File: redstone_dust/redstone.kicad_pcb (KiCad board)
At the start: 2 copper layers, 40 x 40 mm, 76 parts, among them J1 1x4_Pogo, J2 1x4_Pogo, J3 1x4_Pogo, J4 1x4_Pogo, J5 1x4_Pogo, J6 1x4_Pogo, J7 1x4_Pogo, J8 1x4_Pogo, SW1 SW_Push_Open, U1 RP2040

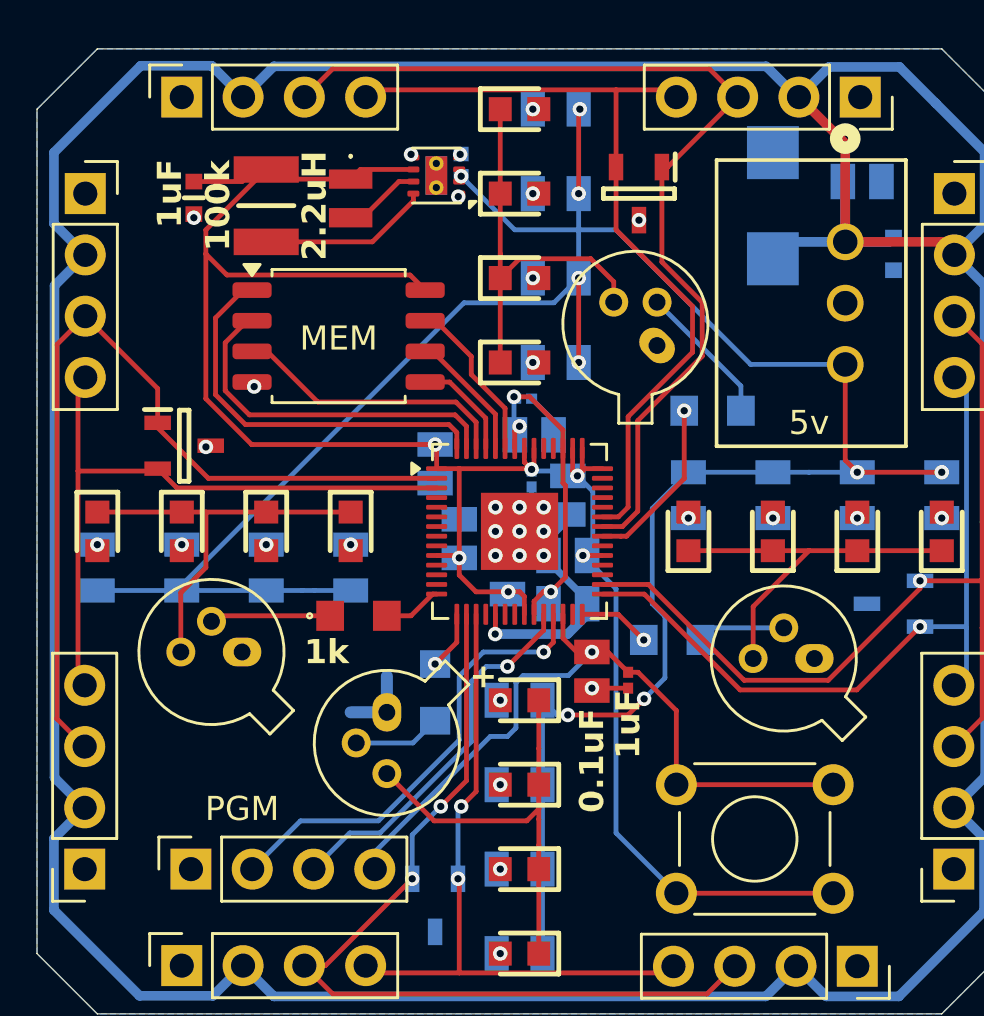
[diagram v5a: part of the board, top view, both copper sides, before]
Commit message: change programming pin 4 to 3.3v
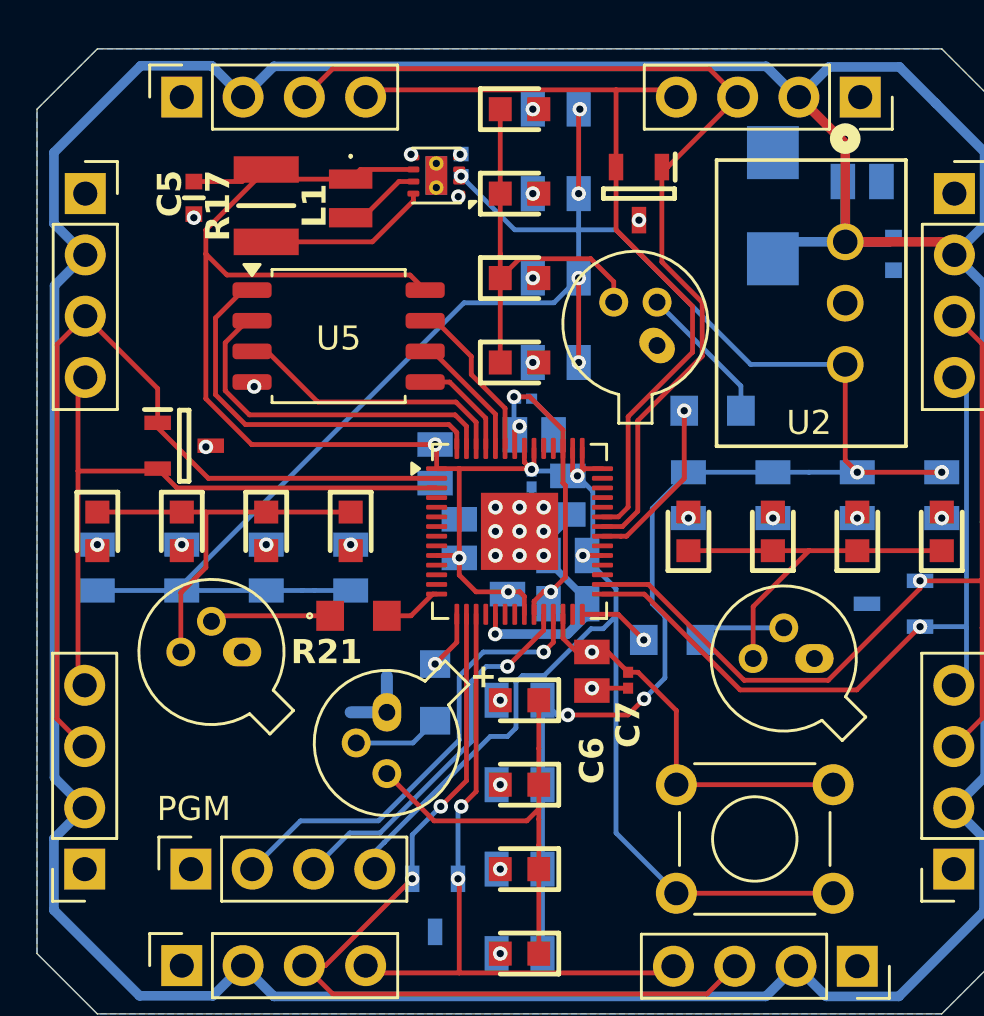
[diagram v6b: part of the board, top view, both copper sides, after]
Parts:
- D5: renamed from - LED +
- D9: renamed from + LED -
- renumbered 10uF to C1, 0.1uF to C2, 0.1uF to C3, 22uF to C4, 1uF to C5, 0.1uF to C6, 1uF to C7, TVS to D19, 2.2uH to L1, BC108 to Q1, BC108 to Q2, BC108 to Q3, BC108 to Q4, 200 to R1, 200 to R11, 200 to R15, 100k to R17, 1k to R18, 1k to R19, 1k to R20, 1k to R21, 200 to R6, 5v to U2, 3.3v to U3, MEM to U5
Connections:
- C6 pad 1: Net-(J9-Pin_4) -> Net-(SW1-B)
- C7 pad 1: Net-(J9-Pin_4) -> Net-(SW1-B)
- PGM pad 4: Net-(J9-Pin_4) -> /3.3V_LOCAL
- SW1 pad 2: Net-(J9-Pin_4) -> Net-(SW1-B)
- U1 pad 26: Net-(J9-Pin_4) -> Net-(SW1-B)
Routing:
- net Net-(J9-Pin_4): track 30.8 -> 0.00 mm, vias 1 -> 0
- net Net-(SW1-B): track 0.00 -> 16.5 mm, vias 0 -> 1
- net /3.3V_LOCAL: track 88.1 -> 104.0 mm
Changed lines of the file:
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@@
 	(net 70 "Net-(U1-GPIO12)")
 	(net 71 "unconnected-(U1-GPIO16-Pad27)")
-	(net 72 "Net-(J9-Pin_4)")
+	(net 72 "Net-(SW1-B)")
 	(net 73 "unconnected-(U1-GPIO9-Pad12)")
 	(net 74 "unconnected-(U1-GPIO8-Pad11)")
@@
 		(descr "150060RS83000")
 		(tags "LED")
-		(property "Reference" "- LED +"
+		(property "Reference" "D5"
 			(at 0 1.5 90)
 			(layer "F.SilkS")
@@
 		(at 148.5 43 -90)
 		(tags "RBT05W24S05 ")
-		(property "Reference" "5v"
+		(property "Reference" "U2"
 			(at 7.5 1.5 0)
 			(unlocked yes)
@@
 			(layers "*.Cu" "*.Mask")
 			(remove_unused_layers no)
-			(net 72 "Net-(J9-Pin_4)")
+			(net 72 "Net-(SW1-B)")
 			(pinfunction "B")
 			(pintype "passive")
@@
 			(layers "*.Cu" "*.Mask")
 			(remove_unused_layers no)
-			(net 72 "Net-(J9-Pin_4)")
+			(net 72 "Net-(SW1-B)")
 			(pinfunction "B")
 			(pintype "passive")
@@
 		(descr "8-Lead Plastic WSON, 2x2mm Body, 0.5mm Pitch, WSON-8, http://www.ti.com/lit/ds/symlink/lm27761.pdf")
 		(tags "WSON 8 1EP ThermalVias")
-		(property "Reference" "3.3v"
+		(property "Reference" "U3"
 			(at 0.05 1.75 0)
 			(layer "F.SilkS")
@@
 		(tags "Through hole socket strip THT 1x04 2.54mm single row")
 		(property "Reference" "PGM"
-			(at 2.5 2.12 180)
+			(at 2.5 0.12 180)
 			(layer "F.SilkS")
 			(effects
@@
 			(layers "*.Cu" "*.Mask")
 			(remove_unused_layers no)
-			(net 72 "Net-(J9-Pin_4)")
+			(net 3 "/3.3V_LOCAL")
 			(pinfunction "Pin_4")
 			(pintype "passive")
@@
 		(descr "GRM03_0.03 L=0.6mm W=0.3mm T=0.3mm")
 		(tags "Capacitor")
-		(property "Reference" "1uF"
+		(property "Reference" "C7"
 			(at 1.83 0 90)
 			(layer "F.SilkS")
@@
 			(size 0.42 0.46)
 			(layers "F.Cu" "F.Mask" "F.Paste")
-			(net 72 "Net-(J9-Pin_4)")
+			(net 72 "Net-(SW1-B)")
 			(pinfunction "1")
 			(pintype "passive")
@@
 		(descr "TO-18-3, generated with kicad-footprint-generator TO_SOT_THT_generate.py")
 		(tags "TO-18-3")
-		(property "Reference" "BC108"
+		(property "Reference" "Q2"
 			(at 1.221961 -1.73 0)
 			(layer "F.SilkS")
@@
 		(descr "LCENA2016MKT2R2M0NK-2")
 		(tags "Inductor")
-		(property "Reference" "2.2uH"
+		(property "Reference" "L1"
 			(at 0.3 1.5 90)
 			(layer "F.SilkS")
@@
 		(descr "ERJUP6")
 		(tags "Resistor")
-		(property "Reference" "1k"
+		(property "Reference" "R21"
 			(at -1.325 1.5 0)
 			(layer "F.SilkS")
@@
 		(descr "GRM18x")
 		(tags "Capacitor")
-		(property "Reference" "1uF"
+		(property "Reference" "C5"
 			(at -0.175 1 270)
 			(layer "F.SilkS")
@@
 		(descr "1210 (3225 Metric)")
 		(tags "Resistor")
-		(property "Reference" "100k"
+		(property "Reference" "R17"
 			(at 0 2 90)
 			(layer "F.SilkS")
@@
 		(descr "TO-18-3, generated with kicad-footprint-generator TO_SOT_THT_generate.py")
 		(tags "TO-18-3")
-		(property "Reference" "BC108"
+		(property "Reference" "Q1"
 			(at 1.411421 -0.992742 0)
 			(layer "F.SilkS")
@@
 		(descr "150060RS83000")
 		(tags "LED")
-		(property "Reference" "+ LED -"
+		(property "Reference" "D9"
 			(at 0 5 0)
 			(layer "F.SilkS")
@@
 		(descr "SOIC, 8 Pin (JEITA/EIAJ ED-7311-19 variation 08-001-BBA and Atmel/Microchip, 208 mils width, https://www.jeita.or.jp/japanese/standard/book/ED-7311-19/#target/page_no=21, https://ww1.microchip.com/downloads/en/DeviceDoc/20005045C.pdf#page=23, https://ww1.microchip.com/downloads/en/DeviceDoc/doc2535.pdf#page=162), generated with kicad-footprint-generator ipc_gullwing_generator.py")
 		(tags "SOIC SO P-SOP SOP SOP-8 SO SO-8 8S2 S2AE/F K04-056 CASE-751BE SO8W 8-Pin-SOIC PSA W8-2 W8-4 W8MS-1 FPT-8P-M08")
-		(property "Reference" "MEM"
+		(property "Reference" "U5"
 			(at 0 0.095 0)
 			(layer "F.SilkS")
@@
 			(layers "F.Cu" "F.Mask" "F.Paste")
 			(roundrect_rratio 0.25)
-			(net 72 "Net-(J9-Pin_4)")
+			(net 72 "Net-(SW1-B)")
 			(pinfunction "RUN")
 			(pintype "input")
@@
 		(descr "C0805F104K")
 		(tags "Capacitor")
-		(property "Reference" "0.1uF"
+		(property "Reference" "C6"
 			(at 3.7 0 270)
 			(layer "F.SilkS")
@@
 			(size 1.02 1.47)
 			(layers "F.Cu" "F.Mask" "F.Paste")
-			(net 72 "Net-(J9-Pin_4)")
+			(net 72 "Net-(SW1-B)")
 			(pinfunction "1")
 			(pintype "passive")
@@
 		(descr "TO-18-3, generated with kicad-footprint-generator TO_SOT_THT_generate.py")
 		(tags "TO-18-3")
-		(property "Reference" "BC108"
+		(property "Reference" "Q3"
 			(at 1.27 -1.5 90)
 			(layer "F.SilkS")
@@
 		(descr "TO-18-3, generated with kicad-footprint-generator TO_SOT_THT_generate.py")
 		(tags "TO-18-3")
-		(property "Reference" "BC108"
+		(property "Reference" "Q4"
 			(at 1.27 -1.5 0)
 			(layer "F.SilkS")
@@
 		(descr "TNPW0805 e3")
 		(tags "Resistor")
-		(property "Reference" "200"
+		(property "Reference" "R15"
 			(at 0 -1.5 90)
 			(layer "B.SilkS")
@@
 		(descr "TNPW0805 e3")
 		(tags "Resistor")
-		(property "Reference" "200"
+		(property "Reference" "R11"
 			(at 0 -2 0)
 			(layer "B.SilkS")
@@
 		(descr "GRM15_0.10 L=1.0mm W=0.5mm T=0.5mm")
 		(tags "Capacitor")
-		(property "Reference" "10uF"
+		(property "Reference" "C1"
 			(at -0.18 1.42 270)
 			(layer "B.SilkS")
@@
 		(descr "C0805F104K")
 		(tags "Capacitor")
-		(property "Reference" "0.1uF"
+		(property "Reference" "C2"
 			(at -0.2 0 90)
 			(layer "B.SilkS")
@@
 		(descr "TNPW0805 e3")
 		(tags "Resistor")
-		(property "Reference" "200"
+		(property "Reference" "R6"
 			(at 0 1.5 90)
 			(layer "B.SilkS")
@@
 		(descr "TNPW0805 e3")
 		(tags "Resistor")
-		(property "Reference" "200"
+		(property "Reference" "R1"
 			(at 0 -5.5 0)
 			(layer "B.SilkS")
@@
 		(descr "C0805F104K")
 		(tags "Capacitor")
-		(property "Reference" "0.1uF"
+		(property "Reference" "C3"
 			(at 2.3 -1.5 0)
 			(layer "B.SilkS")
@@
 		(descr "DO-214AA (SMB)")
 		(tags "TVS Diode (Uni-directional)")
-		(property "Reference" "TVS"
+		(property "Reference" "D19"
 			(at 0 0 0)
 			(layer "B.SilkS")
@@
 		(descr "ERJUP6")
 		(tags "Resistor")
-		(property "Reference" "1k"
+		(property "Reference" "R18"
 			(at -3 0 180)
 			(layer "B.SilkS")
@@
 		(descr "ERJUP6")
 		(tags "Resistor")
-		(property "Reference" "1k"
+		(property "Reference" "R19"
 			(at -1.175 1.5 180)
 			(layer "B.SilkS")
@@
 		(descr "ERJUP6")
 		(tags "Resistor")
-		(property "Reference" "1k"
+		(property "Reference" "R20"
 			(at 2.675 0 90)
 			(layer "B.SilkS")
@@
 		(descr "GRM18x")
 		(tags "Capacitor")
-		(property "Reference" "22uF"
+		(property "Reference" "C4"
 			(at 3 0 270)
 			(layer "B.SilkS")
@@
 	)
 	(segment
+		(start 135.124943 60.974)
+		(end 134.851 61.247943)
+		(width 0.2)
+		(layer "B.Cu")
+		(net 3)
+	)
+	(segment
+		(start 134.851 63.149)
+		(end 134.5 63.5)
+		(width 0.2)
+		(layer "B.Cu")
+		(net 3)
+	)
+	(segment
+		(start 139 58.5)
+		(end 139 67.5)
+		(width 0.2)
+		(layer "B.Cu")
+		(net 3)
+	)
+	(segment
 		(start 135.5 52.5)
 		(end 136.8 52.5)
@@
 	)
 	(segment
+		(start 129.3852 67.901)
+		(end 129.383785 67.901)
+		(width 0.2)
+		(layer "B.Cu")
+		(net 3)
+	)
+	(segment
+		(start 129 68.284785)
+		(end 129 69)
+		(width 0.2)
+		(layer "B.Cu")
+		(net 3)
+	)
+	(segment
+		(start 136.026 60.974)
+		(end 135.124943 60.974)
+		(width 0.2)
+		(layer "B.Cu")
+		(net 3)
+	)
+	(segment
+		(start 133.7862 63.5)
+		(end 129.3852 67.901)
+		(width 0.2)
+		(layer "B.Cu")
+		(net 3)
+	)
+	(segment
 		(start 136.8 52.5)
 		(end 137 52.7)
@@
 	)
 	(segment
+		(start 134.5 63.5)
+		(end 133.7862 63.5)
+		(width 0.2)
+		(layer "B.Cu")
+		(net 3)
+	)
+	(segment
+		(start 137.964 59.036)
+		(end 136.026 60.974)
+		(width 0.2)
+		(layer "B.Cu")
+		(net 3)
+	)
+	(segment
+		(start 139 58.5)
+		(end 138.464 59.036)
+		(width 0.2)
+		(layer "B.Cu")
+		(net 3)
+	)
+	(segment
 		(start 138.036 53.336)
 		(end 137.4 52.7)
@@
 	)
 	(segment
+		(start 138.464 59.036)
+		(end 137.964 59.036)
+		(width 0.2)
+		(layer "B.Cu")
+		(net 3)
+	)
+	(segment
 		(start 139 57.375436)
-		(end 139 67.5)
+		(end 139 58.5)
+		(width 0.2)
+		(layer "B.Cu")
+		(net 3)
+	)
+	(segment
+		(start 134.851 61.247943)
+		(end 134.851 63.149)
 		(width 0.2)
 		(layer "B.Cu")
@@
 	)
 	(segment
+		(start 129.383785 67.901)
+		(end 129 68.284785)
+		(width 0.2)
+		(layer "B.Cu")
+		(net 3)
+	)
+	(segment
 		(start 152.485 43)
 		(end 153.025 43.54)
@@
 		(net 72)
 	)
-	(segment
-		(start 137.026 60.974)
-		(end 135.149 60.974)
-		(width 0.2)
-		(layer "B.Cu")
-		(net 72)
-	)
-	(segment
-		(start 134.851 63.149)
-		(end 134.5 63.5)
-		(width 0.2)
-		(layer "B.Cu")
-		(net 72)
-	)
-	(segment
-		(start 134.5 63.5)
-		(end 133.7862 63.5)
-		(width 0.2)
-		(layer "B.Cu")
-		(net 72)
-	)
-	(segment
-		(start 135.149 60.974)
-		(end 134.851 61.272)
-		(width 0.2)
-		(layer "B.Cu")
-		(net 72)
-	)
-	(segment
-		(start 133.7862 63.5)
-		(end 129 68.2862)
-		(width 0.2)
-		(layer "B.Cu")
-		(net 72)
-	)
-	(segment
-		(start 138 60)
-		(end 137.026 60.974)
-		(width 0.2)
-		(layer "B.Cu")
-		(net 72)
-	)
-	(segment
-		(start 129 68.2862)
-		(end 129 69)
-		(width 0.2)
-		(layer "B.Cu")
-		(net 72)
-	)
-	(segment
-		(start 134.851 61.272)
-		(end 134.851 63.149)
-		(width 0.2)
-		(layer "B.Cu")
-		(net 72)
-	)
